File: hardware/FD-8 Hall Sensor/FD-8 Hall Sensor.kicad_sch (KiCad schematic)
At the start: 11 parts, among them J1 Conn_01x03_Socket, J2 Conn_01x02_Socket, J3 Conn_02x03_Odd_Even, U1 ATtiny13A-P, U2 MCP42100, U3 LM2936-5.0

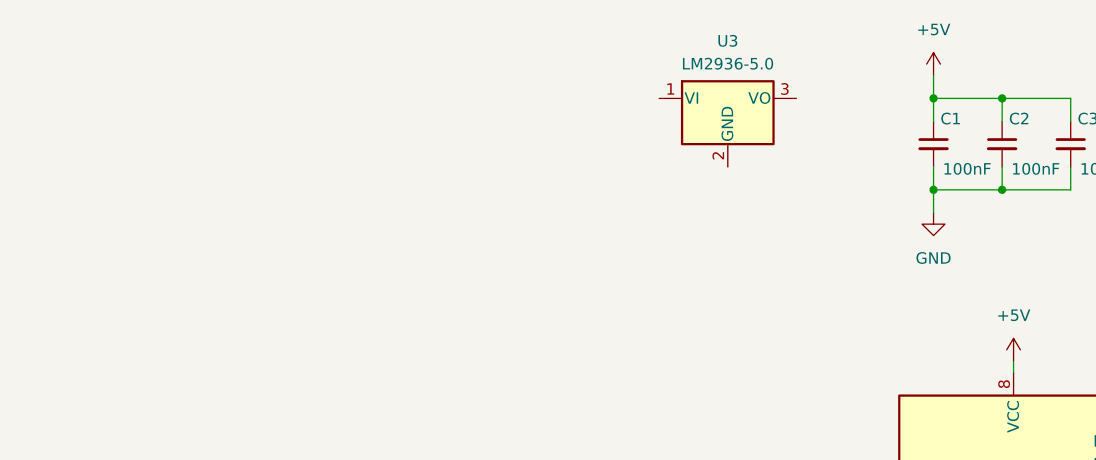
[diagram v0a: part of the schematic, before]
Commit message: add LM2940T, finish power section
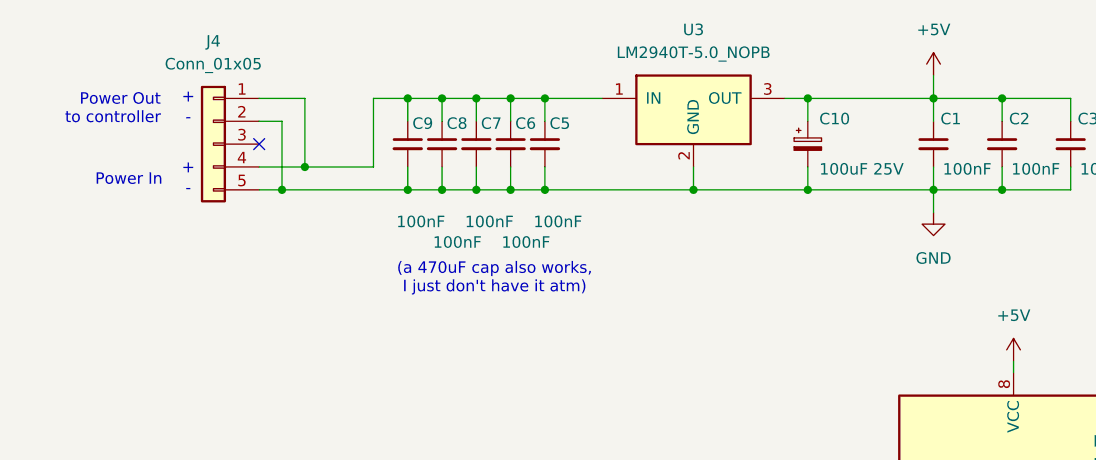
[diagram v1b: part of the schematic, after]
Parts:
- removed U3: LM2936-5.0, symbol Regulator_Linear:LM2936-5.0
- added C10: 100uF 25V, symbol Device:C_Polarized_Small
- added C5, C6, C7, C8, C9: 100nF, symbol Device:C_Small
- added J4: Conn_01x05, symbol Connector_Generic:Conn_01x05
- added U3: LM2940T-5.0_NOPB, TO_SOT_Packages_THT:TO-220_Vertical, symbol LM2940T-5.0_NOPB:LM2940T-5.0_NOPB
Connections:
- net +5V: now also C10.1, U3.3 (OUT)
- net GND: now also C10.2, C5.2, C6.2, C7.2, C8.2, C9.2, J4.2 (Pin_2), J4.5 (Pin_5), U3.2 (GND)
- new net: C5.1, C6.1, C7.1, C8.1, C9.1, J4.1 (Pin_1), J4.4 (Pin_4), U3.1 (IN)
- no-connect marks 4 -> 5
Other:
- note added: "(a 470uF cap also works, I just don't have it atm)"
- note added: "+"
- note added: "-"
- note added: "Power In"
- note added: "Power Out to controller"

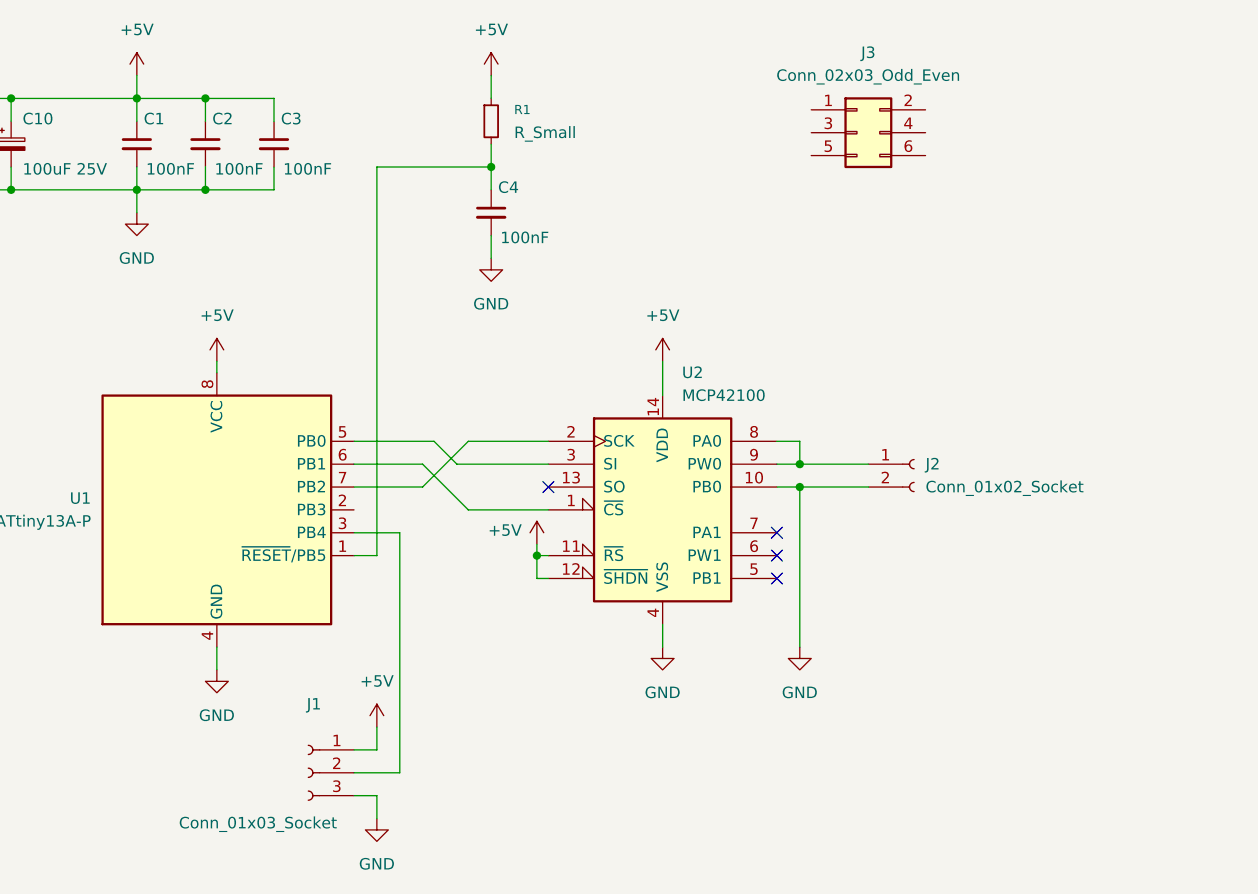
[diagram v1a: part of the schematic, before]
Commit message: add remaining components to schematic
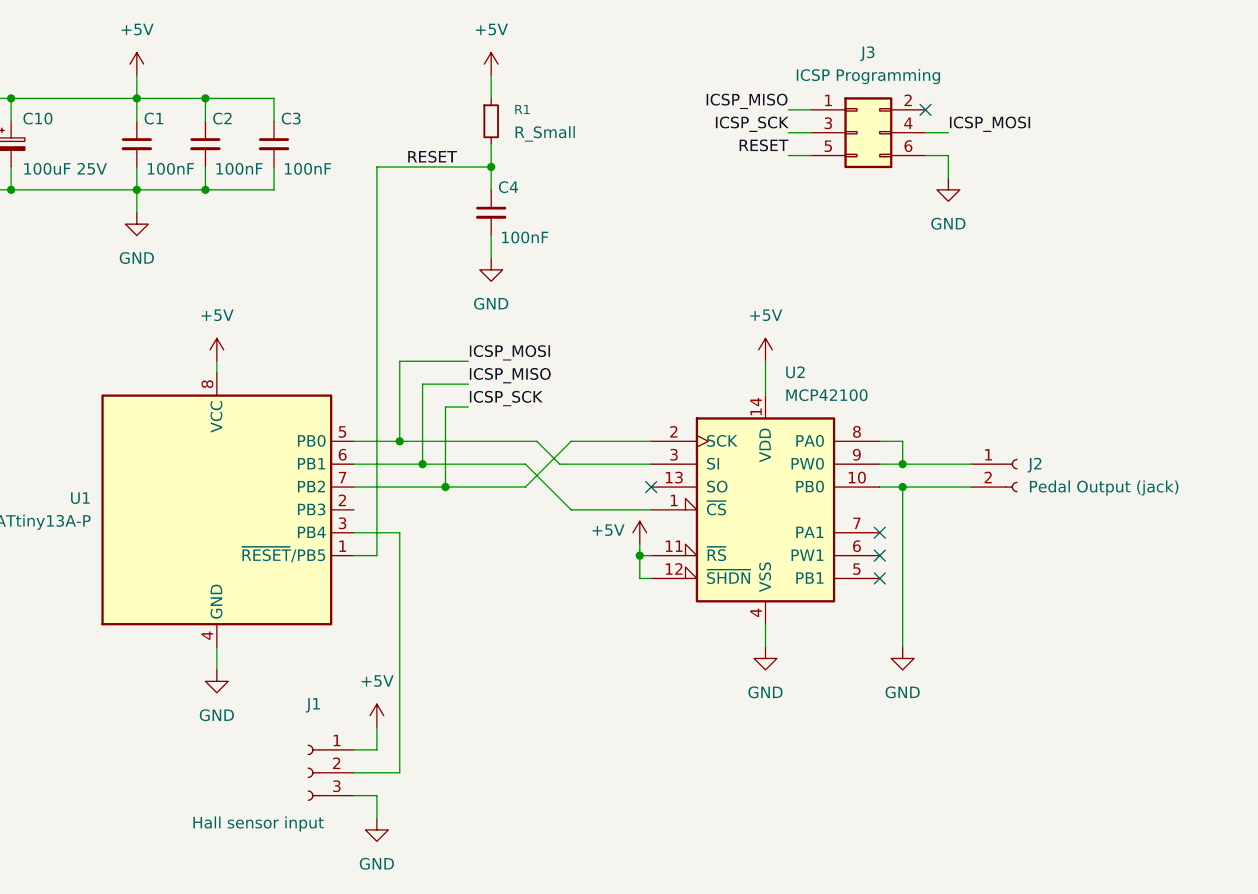
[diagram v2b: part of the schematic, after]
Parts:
- J1: value Conn_01x03_Socket -> Hall sensor input
- J2: value Conn_01x02_Socket -> Pedal Output (jack)
- J3: value Conn_02x03_Odd_Even -> ICSP Programming
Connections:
- net GND: now also J3.6 (Pin_6)
- net RESET: now reaches C4.1, R1.2, U1.1 (~{RESET}/PB5)
- net RESET: now also J3.5 (Pin_5)
- net ICSP_MOSI: now reaches U1.5 (PB0), U2.3 (SI)
- net ICSP_MOSI: now also J3.4 (Pin_4)
- net ICSP_MISO: now reaches U1.6 (PB1), U2.1 (~{CS})
- net ICSP_MISO: now also J3.1 (Pin_1)
- net ICSP_SCK: now reaches U1.7 (PB2), U2.2 (SCK)
- net ICSP_SCK: now also J3.3 (Pin_3)
- no-connect marks 5 -> 6
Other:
- moved on the sheet: J2, U2

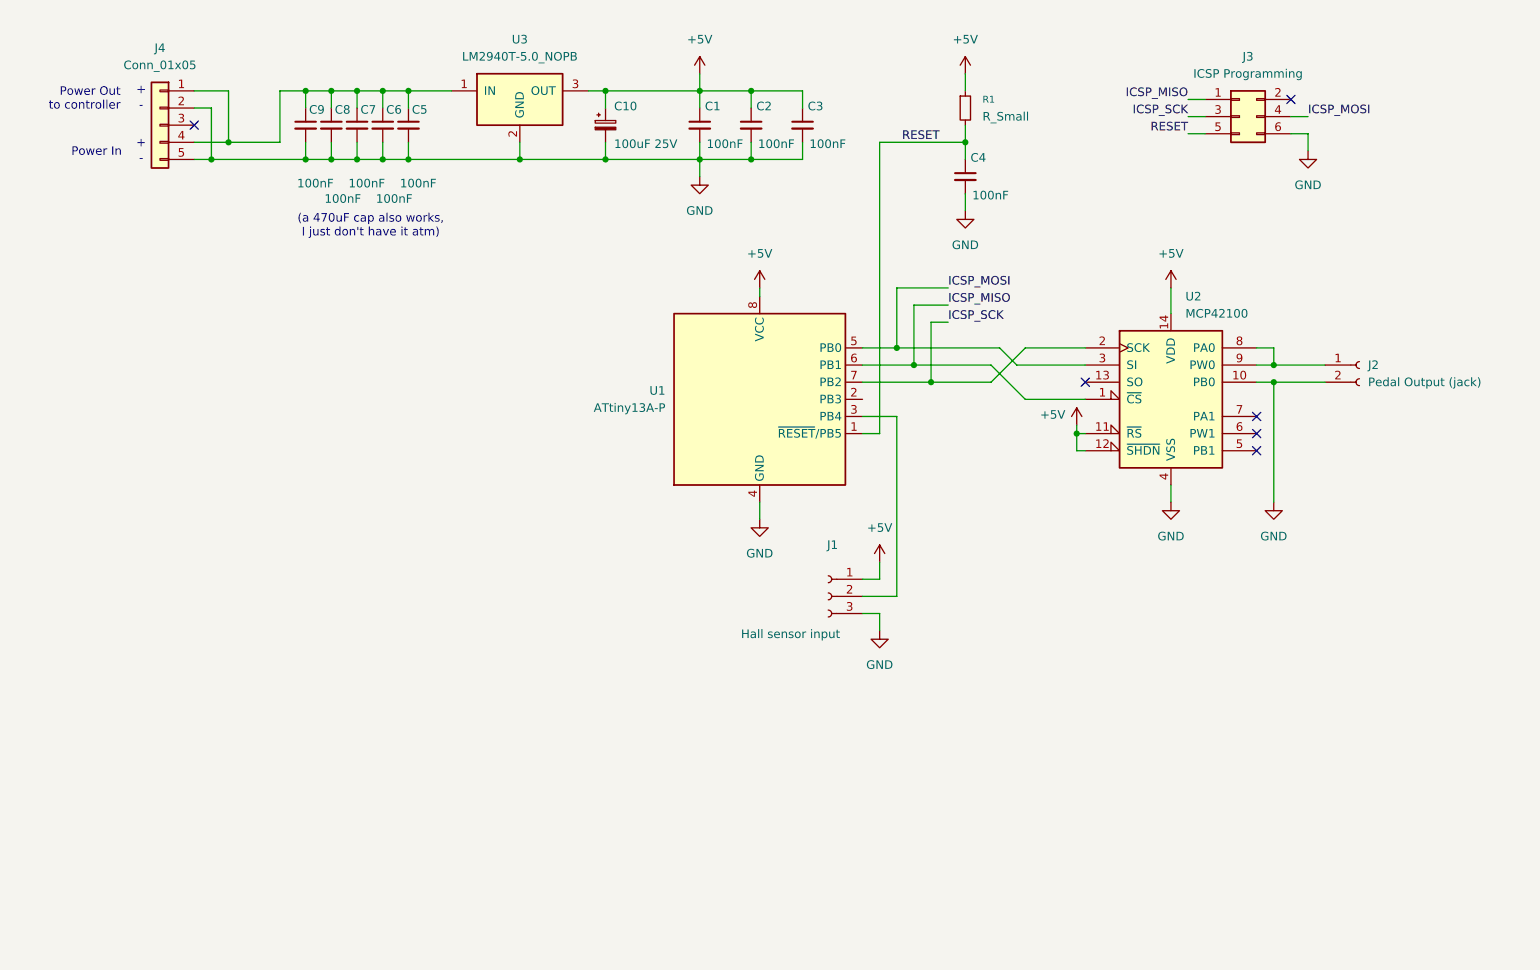
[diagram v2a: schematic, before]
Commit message: fix schematic, pair footprints
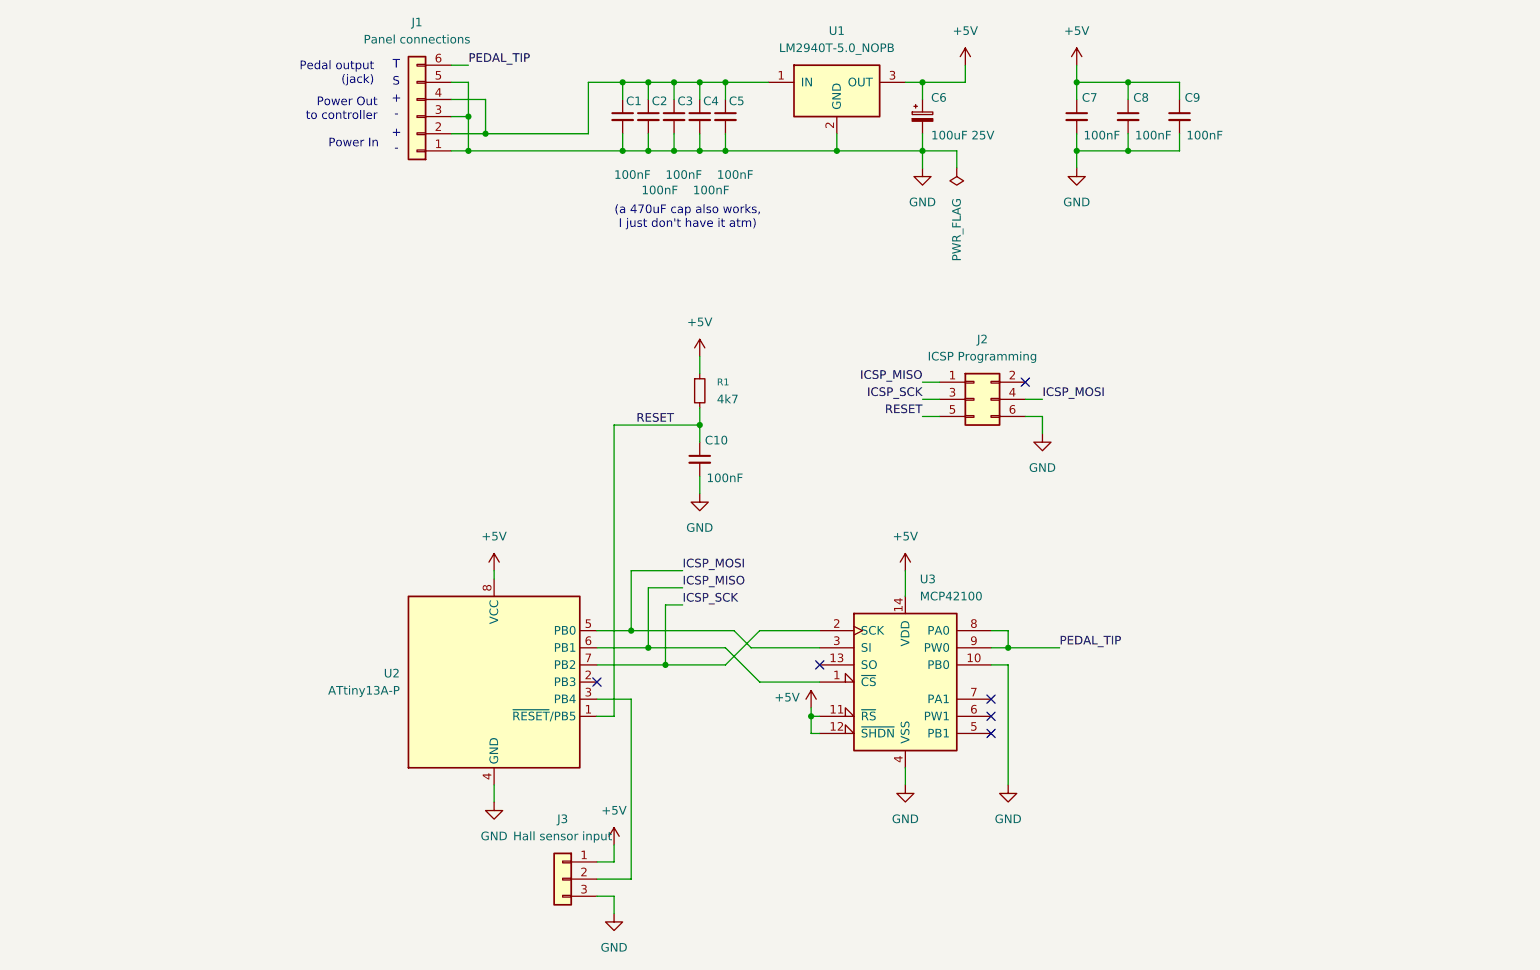
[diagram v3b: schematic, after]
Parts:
- removed J1: Hall sensor input, symbol Connector:Conn_01x03_Socket
- removed J2: Pedal Output (jack), symbol Connector:Conn_01x02_Socket
- removed J4: Conn_01x05, symbol Connector_Generic:Conn_01x05
- added J1: Panel connections, Connector_Molex:Molex_KK-254_AE-6410-06A_1x06_P2.54mm_Vertical, symbol Connector_Generic:Conn_01x06
- added J3: Hall sensor input, Connector_Molex:Molex_KK-254_AE-6410-03A_1x03_P2.54mm_Vertical, symbol Connector_Generic:Conn_01x03
- C1: renamed from C9; footprint (none) -> Capacitor_THT:C_Disc_D4.7mm_W2.5mm_P5.00mm
- C10: renamed from C4; footprint (none) -> Capacitor_THT:C_Disc_D4.7mm_W2.5mm_P5.00mm
- C2: renamed from C8; footprint (none) -> Capacitor_THT:C_Disc_D4.7mm_W2.5mm_P5.00mm
- C3: renamed from C7; footprint (none) -> Capacitor_THT:C_Disc_D4.7mm_W2.5mm_P5.00mm
- C4: renamed from C6; footprint (none) -> Capacitor_THT:C_Disc_D4.7mm_W2.5mm_P5.00mm
- C5: footprint (none) -> Capacitor_THT:C_Disc_D4.7mm_W2.5mm_P5.00mm
- C6: renamed from C10; footprint (none) -> Capacitor_THT:CP_Radial_D5.0mm_P2.50mm
- C7: renamed from C1; footprint (none) -> Capacitor_THT:C_Disc_D4.7mm_W2.5mm_P5.00mm
- C8: renamed from C2; footprint (none) -> Capacitor_THT:C_Disc_D4.7mm_W2.5mm_P5.00mm
- C9: renamed from C3; footprint (none) -> Capacitor_THT:C_Disc_D4.7mm_W2.5mm_P5.00mm
- J2: renamed from J3; footprint (none) -> Connector_PinHeader_2.54mm:PinHeader_2x03_P2.54mm_Vertical
- R1: value R_Small -> 4k7; footprint (none) -> Resistor_THT:R_Axial_DIN0207_L6.3mm_D2.5mm_P10.16mm_Horizontal
- U1: renamed from U3; footprint TO_SOT_Packages_THT:TO-220_Vertical -> Package_TO_SOT_THT:TO-220-3_Vertical
- U3: renamed from U2; footprint (none) -> Package_DIP:DIP-14_W7.62mm
- renumbered U1 to U2
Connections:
- net +5V: now also J3.1 (Pin_1)
- net GND: now also J1.1 (Pin_1), J1.3 (Pin_3), J1.5 (Pin_5), J3.3 (Pin_3)
- net at C1.1, C2.1, C3.1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: now also J1.2 (Pin_2), J1.4 (Pin_4)
- net at U2.3 (PB4): now also J3.2 (Pin_2)
- net PEDAL_TIP: now reaches U3.8 (PA0), U3.9 (PW0)
- net PEDAL_TIP: now also J1.6 (Pin_6)
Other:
- note added: "Pedal output (jack)"
- note added: "S"
- note added: "T"
- moved on the sheet: C1, C10, C2, C3, C4, C5, C6, C7, C8, C9, J2, R1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

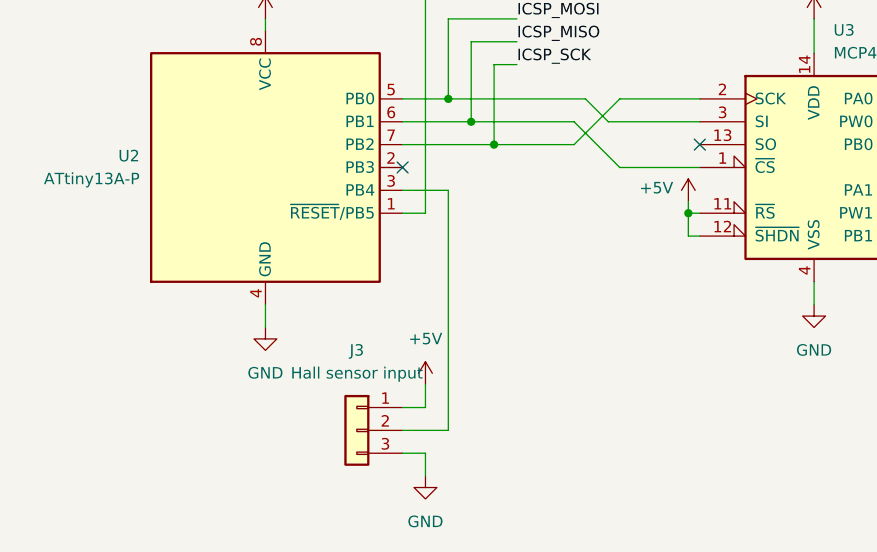
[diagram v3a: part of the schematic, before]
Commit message: add extra GPIO header
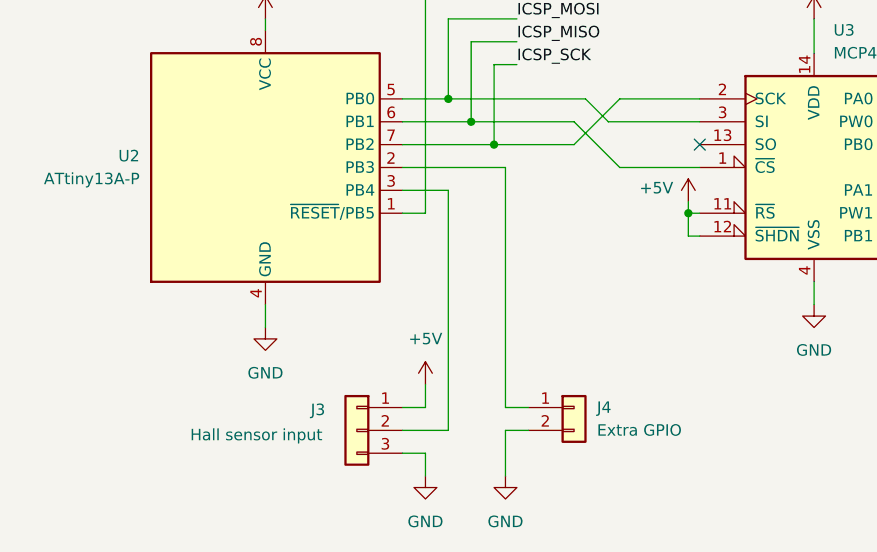
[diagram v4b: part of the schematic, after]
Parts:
- added J4: Extra GPIO, Connector_PinHeader_2.54mm:PinHeader_1x02_P2.54mm_Vertical, symbol Connector_Generic:Conn_01x02
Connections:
- net GND: now also J4.2 (Pin_2)
- net at U2.2 (PB3): now also J4.1 (Pin_1)
- no-connect marks 6 -> 5
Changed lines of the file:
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@@
 	)
 	(no_connect
-		(at 111.76 132.08)
-	)
-	(no_connect
 		(at 144.78 129.54)
 	)
@@
 	(wire
 		(pts
+			(xy 111.76 132.08) (xy 123.19 132.08)
+		)
+		(stroke
+			(width 0)
+			(type default)
+		)
+	)
+	(wire
+		(pts
 			(xy 119.38 118.11) (xy 119.38 127)
 		)
@@
 	(wire
 		(pts
+			(xy 123.19 161.29) (xy 123.19 166.37)
+		)
+		(stroke
+			(width 0)
+			(type default)
+		)
+	)
+	(wire
+		(pts
 			(xy 111.76 127) (xy 119.38 127)
 		)
@@
 	(wire
 		(pts
+			(xy 123.19 132.08) (xy 123.19 158.75)
+		)
+		(stroke
+			(width 0)
+			(type default)
+		)
+	)
+	(wire
+		(pts
 			(xy 127 93.98) (xy 127 96.52)
 		)
@@
 	(wire
 		(pts
+			(xy 123.19 158.75) (xy 125.73 158.75)
+		)
+		(stroke
+			(width 0)
+			(type default)
+		)
+	)
+	(wire
+		(pts
 			(xy 160.02 53.34) (xy 160.02 55.88)
 		)
@@
 	(wire
 		(pts
+			(xy 123.19 161.29) (xy 125.73 161.29)
+		)
+		(stroke
+			(width 0)
+			(type default)
+		)
+	)
+	(wire
+		(pts
 			(xy 172.72 124.46) (xy 172.72 127)
 		)
@@
 	)
 	(symbol
+		(lib_id "power:GND")
+		(at 123.19 166.37 0)
+		(unit 1)
+		(exclude_from_sim no)
+		(in_bom yes)
+		(on_board yes)
+		(dnp no)
+		(fields_autoplaced yes)
+		(property "Reference" "#PWR016"
+			(at 123.19 172.72 0)
+			(effects
+				(font
+					(size 1.27 1.27)
+				)
+				(hide yes)
+			)
+		)
+		(property "Value" "GND"
+			(at 123.19 171.45 0)
+			(effects
+				(font
+					(size 1.27 1.27)
+				)
+			)
+		)
+		(property "Footprint" ""
+			(at 123.19 166.37 0)
+			(effects
+				(font
+					(size 1.27 1.27)
+				)
+				(hide yes)
+			)
+		)
+		(property "Datasheet" ""
+			(at 123.19 166.37 0)
+			(effects
+				(font
+					(size 1.27 1.27)
+				)
+				(hide yes)
+			)
+		)
+		(property "Description" "Power symbol creates a global label with name \"GND\" , ground"
+			(at 123.19 166.37 0)
+			(effects
+				(font
+					(size 1.27 1.27)
+				)
+				(hide yes)
+			)
+		)
+		(pin "1"
+		)
+		(instances
+			(project "FD-8 Hall Sensor"
+				(path "/5366db3b-dbed-4029-8870-4667f57d6295"
+					(reference "#PWR016")
+					(unit 1)
+				)
+			)
+		)
+	)
+	(symbol
 		(lib_id "Device:R_Small")
 		(at 127 88.9 0)
@@
 	)
 	(symbol
+		(lib_id "Connector_Generic:Conn_01x02")
+		(at 130.81 158.75 0)
+		(unit 1)
+		(exclude_from_sim no)
+		(in_bom yes)
+		(on_board yes)
+		(dnp no)
+		(fields_autoplaced yes)
+		(property "Reference" "J4"
+			(at 133.35 158.7499 0)
+			(effects
+				(font
+					(size 1.27 1.27)
+				)
+				(justify left)
+			)
+		)
+		(property "Value" "Extra GPIO"
+			(at 133.35 161.2899 0)
+			(effects
+				(font
+					(size 1.27 1.27)
+				)
+				(justify left)
+			)
+		)
+		(property "Footprint" "Connector_PinHeader_2.54mm:PinHeader_1x02_P2.54mm_Vertical"
+			(at 130.81 158.75 0)
+			(effects
+				(font
+					(size 1.27 1.27)
+				)
+				(hide yes)
+			)
+		)
+		(property "Datasheet" "~"
+			(at 130.81 158.75 0)
+			(effects
+				(font
+					(size 1.27 1.27)
+				)
+				(hide yes)
+			)
+		)
+		(property "Description" "Generic connector, single row, 01x02, script generated (kicad-library-utils/schlib/autogen/connector/)"
+			(at 130.81 158.75 0)
+			(effects
+				(font
+					(size 1.27 1.27)
+				)
+				(hide yes)
+			)
+		)
+		(pin "1"
+		)
+		(pin "2"
+		)
+		(instances
+			(project ""
+				(path "/5366db3b-dbed-4029-8870-4667f57d6295"
+					(reference "J4")
+					(unit 1)
+				)
+			)
+		)
+	)
+	(symbol
 		(lib_id "power:+5V")
 		(at 157.48 115.57 0)
@@
 		(on_board yes)
 		(dnp no)
-		(fields_autoplaced yes)
 		(property "Reference" "J3"
-			(at 106.68 152.4 0)
+			(at 102.362 159.004 0)
 			(effects
 				(font
@@
 		)
 		(property "Value" "Hall sensor input"
-			(at 106.68 154.94 0)
+			(at 95.504 161.798 0)
 			(effects
 				(font
